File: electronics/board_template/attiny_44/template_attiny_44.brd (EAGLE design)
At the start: 48 x 48 mm, 16 parts, among them IC2 ATTINY44A-MU, IC3 NCP1117ST50T3G, J1 GROVE_CONNECTOR2.0_1X4, J2 GROVE_CONNECTOR2.0_1X4, J3 10129383-906001ALF, Y1 X322516MLB4SI

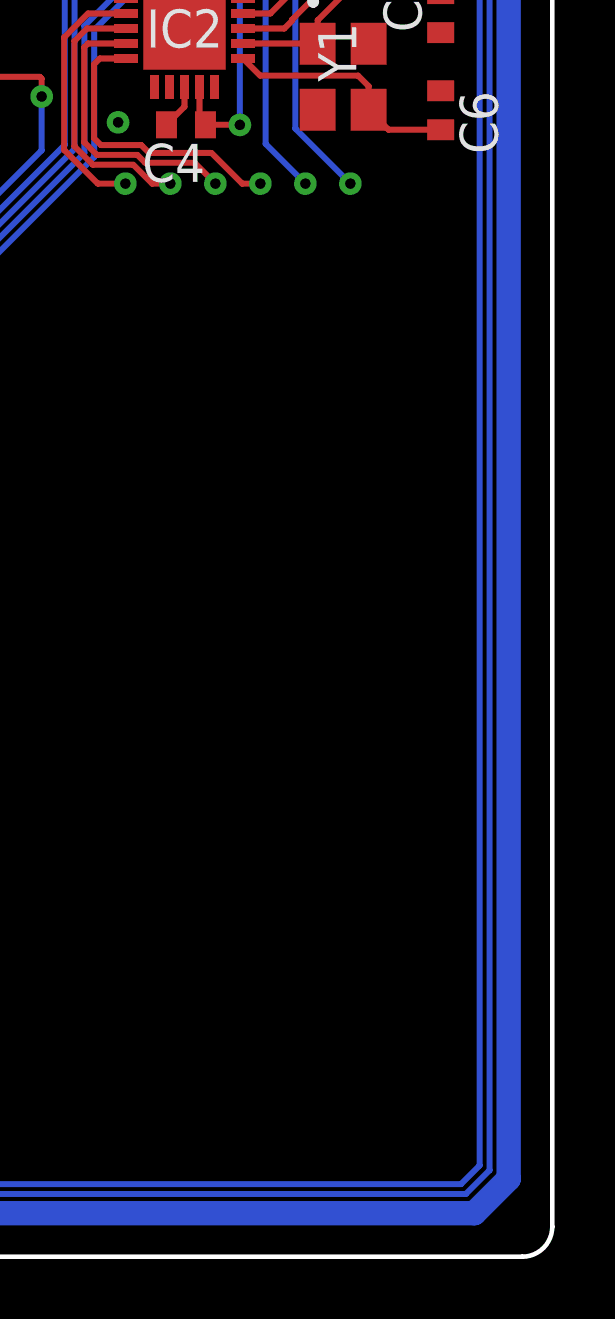
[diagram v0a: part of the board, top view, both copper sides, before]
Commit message: Logo hinzugefügt
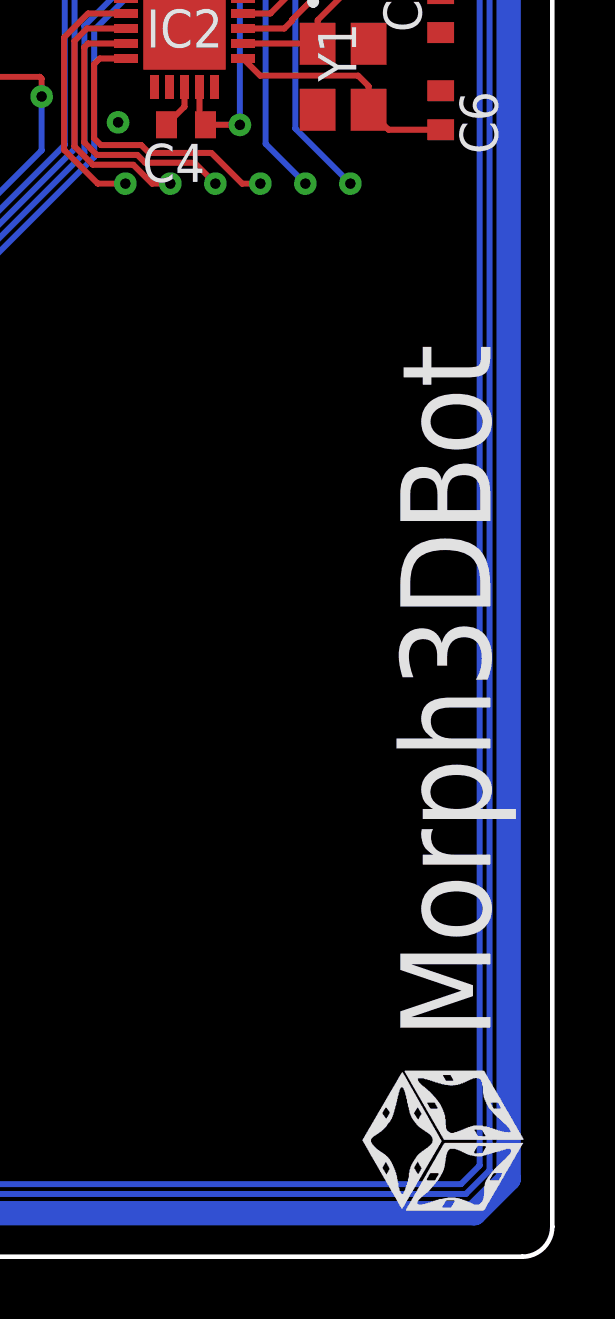
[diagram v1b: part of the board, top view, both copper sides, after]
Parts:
- added U$1: LOGO_MORPHBOT5MM, topo-eng:LOGO_MORPHBOT
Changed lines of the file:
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@@
 <layer number="104" name="Name" color="7" fill="1" visible="no" active="yes"/>
 <layer number="116" name="Patch_BOT" color="9" fill="4" visible="no" active="yes"/>
+<layer number="120" name="brd_placement_notes" color="7" fill="1" visible="yes" active="yes"/>
 <layer number="121" name="_tsilk" color="7" fill="1" visible="no" active="yes"/>
 <layer number="122" name="_bsilk" color="7" fill="1" visible="no" active="yes"/>
+<layer number="144" name="DrillLegend" color="7" fill="1" visible="yes" active="yes"/>
+<layer number="145" name="DrillLegend_01-16" color="7" fill="1" visible="yes" active="yes"/>
+<layer number="146" name="DrillLegend_01-20" color="7" fill="1" visible="yes" active="yes"/>
 <layer number="151" name="HeatSink" color="14" fill="1" visible="no" active="no"/>
+<layer number="198" name="BMP198" color="7" fill="1" visible="yes" active="yes"/>
+<layer number="199" name="Contour" color="7" fill="1" visible="yes" active="yes"/>
 <layer number="200" name="200bmp" color="1" fill="10" visible="no" active="no"/>
 <layer number="201" name="201bmp" color="2" fill="1" visible="no" active="no"/>
@@
 <layer number="207" name="207bmp" color="15" fill="10" visible="no" active="no"/>
 <layer number="208" name="208bmp" color="9" fill="10" visible="no" active="yes"/>
+<layer number="209" name="Route9Document" color="7" fill="1" visible="yes" active="yes"/>
+<layer number="210" name="Route10Document" color="7" fill="1" visible="yes" active="yes"/>
+<layer number="211" name="Route11Document" color="7" fill="1" visible="yes" active="yes"/>
+<layer number="212" name="Route12Document" color="7" fill="1" visible="yes" active="yes"/>
+<layer number="213" name="Route13Document" color="7" fill="1" visible="yes" active="yes"/>
+<layer number="214" name="Route14Document" color="7" fill="1" visible="yes" active="yes"/>
+<layer number="215" name="Route15Document" color="7" fill="1" visible="yes" active="yes"/>
+<layer number="216" name="BottomDocument" color="7" fill="1" visible="yes" active="yes"/>
+<layer number="220" name="DimensionDocument" color="7" fill="1" visible="yes" active="yes"/>
+<layer number="221" name="tPlaceDocument" color="7" fill="1" visible="yes" active="yes"/>
+<layer number="222" name="bPlaceDocument" color="7" fill="1" visible="yes" active="yes"/>
+<layer number="225" name="tNamesDocument" color="7" fill="1" visible="yes" active="yes"/>
+<layer number="226" name="bNamesDocument" color="7" fill="1" visible="yes" active="yes"/>
+<layer number="227" name="tValuesDocument" color="7" fill="1" visible="yes" active="yes"/>
+<layer number="228" name="bValuesDocument" color="7" fill="1" visible="yes" active="yes"/>
+<layer number="229" name="tStopDocument" color="7" fill="1" visible="yes" active="yes"/>
+<layer number="230" name="bStopDocument" color="7" fill="1" visible="yes" active="yes"/>
+<layer number="231" name="tCreamDocument" color="7" fill="1" visible="yes" active="yes"/>
+<layer number="232" name="bCreamDocument" color="7" fill="1" visible="yes" active="yes"/>
+<layer number="233" name="tFinishDocument" color="7" fill="1" visible="yes" active="yes"/>
+<layer number="234" name="bFinishDocument" color="7" fill="1" visible="yes" active="yes"/>
+<layer number="235" name="tGlueDocument" color="7" fill="1" visible="yes" active="yes"/>
+<layer number="236" name="bGlueDocument" color="7" fill="1" visible="yes" active="yes"/>
+<layer number="244" name="DrillsDocument" color="7" fill="1" visible="yes" active="yes"/>
+<layer number="245" name="HolesDocument" color="7" fill="1" visible="yes" active="yes"/>
+<layer number="246" name="MillingDocument" color="7" fill="1" visible="yes" active="yes"/>
+<layer number="247" name="MeasuresDocument" color="7" fill="1" visible="yes" active="yes"/>
 <layer number="250" name="Descript" color="3" fill="1" visible="no" active="no"/>
 <layer number="251" name="SMDround" color="12" fill="11" visible="no" active="no"/>
@@
 <attribute name="VALUE" x="18.076159375" y="45.291775" size="1.016" layer="27" rot="R180"/>
 </element>
+<element name="U$1" library="topo-eng" library_urn="urn:adsk.eagle:library:6646478" package="LOGO_MORPHBOT" value="LOGO_MORPHBOT5MM" x="47.143325" y="1.290628125" smashed="yes" rot="R90"/>
 </elements>
 <signals>
